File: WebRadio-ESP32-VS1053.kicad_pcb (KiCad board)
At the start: 2 copper layers, 91.5 x 61 mm, 72 parts, among them J1 Conn_01x02, J2 Conn_01x02_Pin, J3 Conn_01x02_Pin, J4 AudioJack3, J5 Conn_01x02_Pin, SW1 SW_Push, SW2 SW_Push, SW3 SW_Push, SW4 SW_Push, U1 AMS1117-1.8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

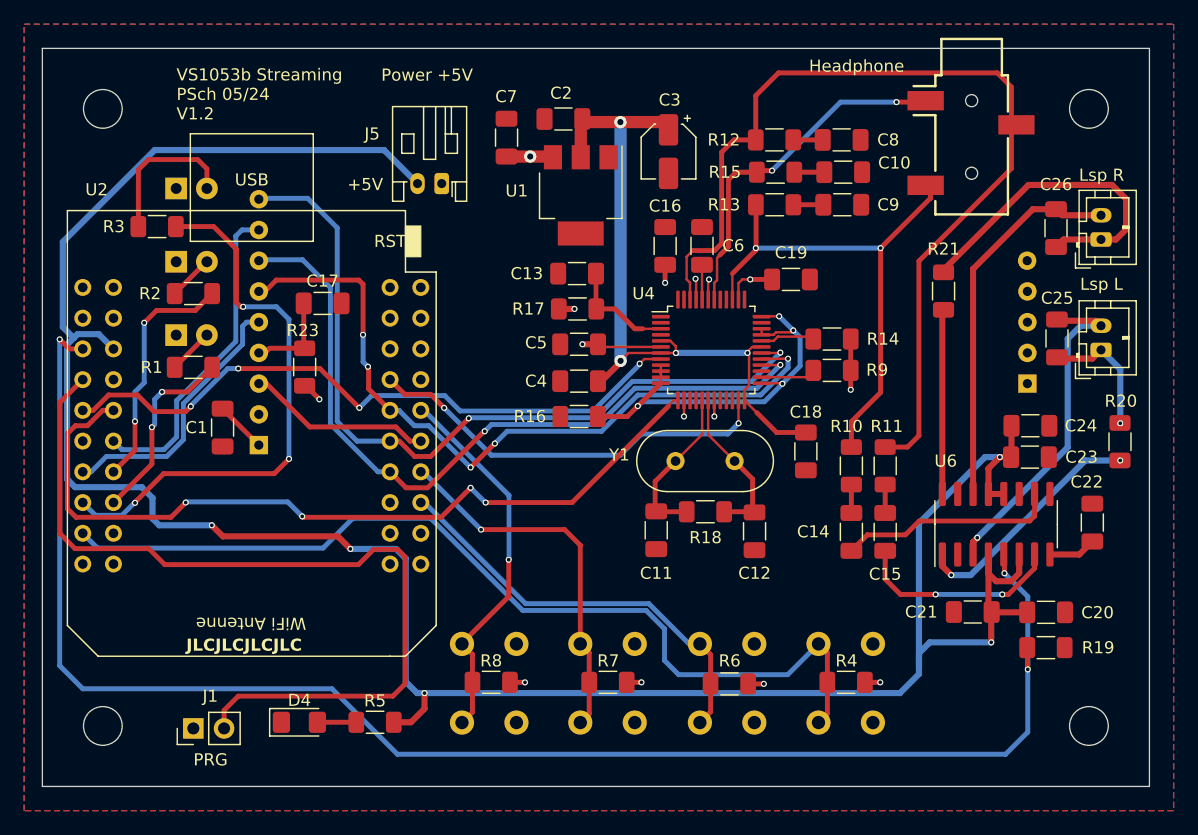
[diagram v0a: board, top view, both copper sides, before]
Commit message: include power over usb-c and jst connector
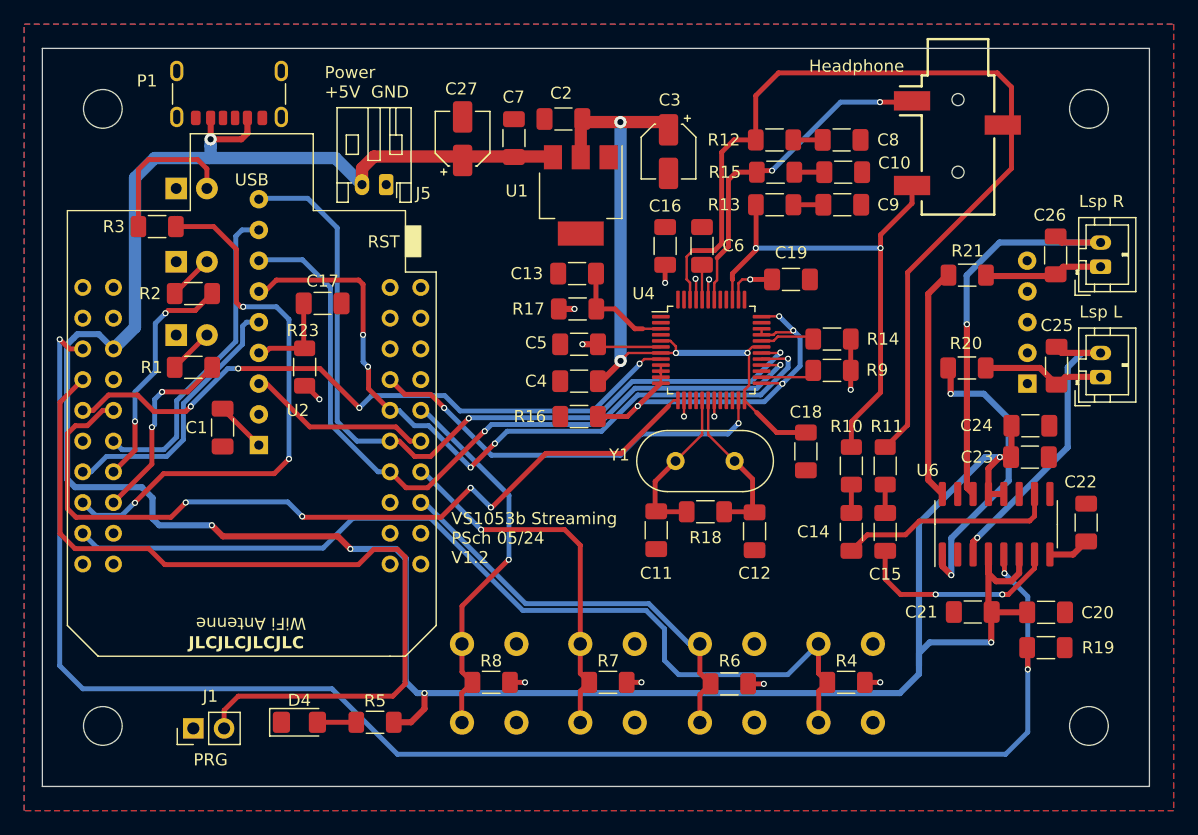
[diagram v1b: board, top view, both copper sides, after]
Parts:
- added C27: 100µF, Capacitor_SMD:CP_Elec_4x5.4, F.Cu at (148.2, 67.5)
- added P1: USB_C_Plug_USB2.0, Connector_USB:USB_C_Receptacle_GCT_USB4125-xx-x_6P_TopMnt_Horizontal, F.Cu at (128.9, 62.7)
- C3: value 10µF -> 47µF
- H1, H2, H3, H4: footprint MountingHole:MountingHole_3.2mm_M3_ISO7380 -> MountingHole:MountingHole_3.2mm_M3_ISO14580
- J4: footprint psch:Jack_3.5mm_SMT_Horizontal -> lib_psch:Jack_3.5mm_SMT_Horizontal
- U2: footprint esp32-mini:ESP32_mini -> ESP32_mini:ESP32_mini
- U5: footprint psch:JLCPCB-Marker -> lib_psch:JLCPCB-Marker
- moved U5 66.3 mm to (130.4, 109.7)
- moved R20 14.0 mm to (189.9, 86.4), turned to 180 degrees
- moved J5 4.59 mm to (141.9, 71.3)
- moved R21 2.36 mm to (189.9, 78.7), turned to 180 degrees
- moved C25 2.25 mm to (197.3, 86.2)
- moved C26 2.25 mm to (197.2, 77.1)
- moved J2 2.25 mm to (201.0, 87.2)
- moved J3 2.25 mm to (201.0, 78.0)
- moved J4 1.13 mm to (189.2, 59.2)
- moved C7 0.61 mm to (152.5, 67.4)
- moved C22 0.51 mm to (199.8, 99.2)
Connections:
- net Net-(U1-VO) renamed +1.8V
- C7 pad 1: +3.3V -> +5V
- U1 pad 3: +3.3V -> +5V
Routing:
- net +5V: track 201.3 -> 220.1 mm, vias 5 -> 6
- net Net-(J3-Pin_1): track 27.6 -> 9.82 mm
- net Net-(U6-LOUT+): track 19.9 -> 24.7 mm
- net Net-(U6-ROUT+): track 15.3 -> 19.4 mm
- net +3.3V: track 39.1 -> 35.1 mm, vias 15 -> 14
- net Net-(J3-Pin_2): track 31.4 -> 34.4 mm, vias 0 -> 1
- net Net-(J2-Pin_2): track 28.1 -> 25.7 mm
- net Net-(U4-GBUF): track 30.9 -> 29.4 mm
- net Net-(U4-LEFT): track 79.0 -> 77.9 mm
- net LED_02: track 20.0 -> 19.4 mm
- net Net-(U4-RIGHT): track 43.7 -> 43.2 mm
- net Net-(U6-VREF): track 3.95 -> 3.44 mm
- net Net-(J2-Pin_1): track 11.2 -> 10.9 mm, vias 1 -> 0
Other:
- board text added: "Power +5V GND"
- board text removed: "Power +5V"

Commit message: change some comments
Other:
- board text added: "WebRadio ESP32 PSch 05/24 V1.2"
- board text removed: "VS1053b Streaming PSch 05/24 V1.2"
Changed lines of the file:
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@@
 		)
 	)
-	(gr_text "VS1053b Streaming\nPSch 05/24\nV1.2"
+	(gr_text "WebRadio ESP32\nPSch 05/24\nV1.2"
 		(at 137.922 110.3376 0)
 		(layer "B.SilkS")
@@
 		)
 	)
-	(gr_text "VS1053b Streaming\nPSch 05/24\nV1.2"
-		(at 147.2946 102.6668 0)
+	(gr_text "WebRadio ESP32\nPSch 05/24\nV1.2"
+		(at 148.5392 102.8192 0)
 		(layer "F.SilkS")
 		(effects

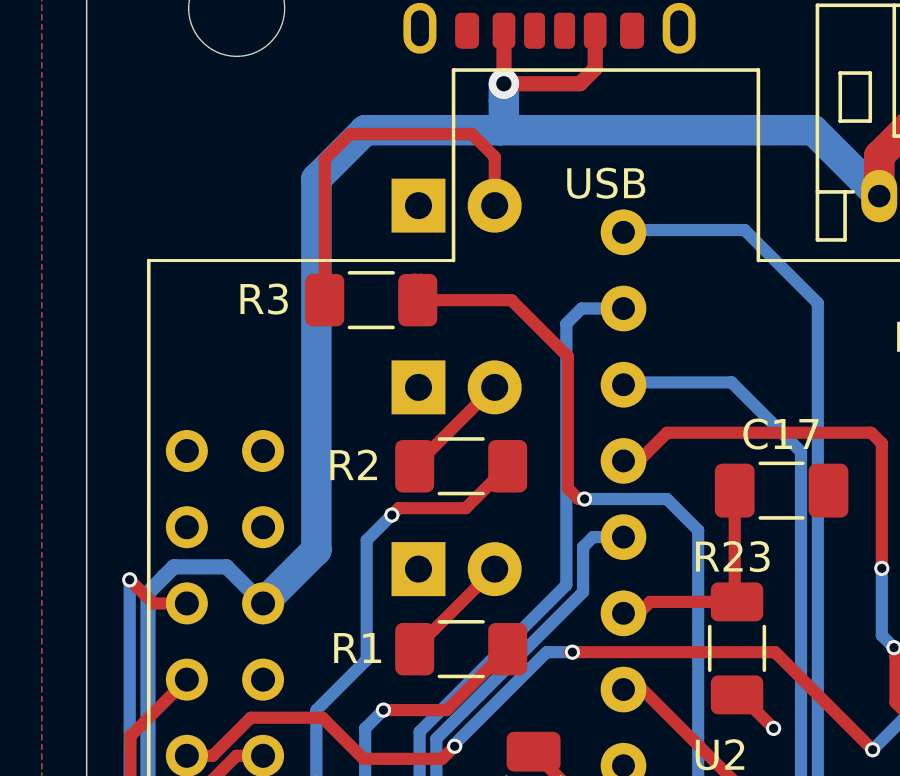
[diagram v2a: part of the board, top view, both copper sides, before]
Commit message: add new footrint for 3mm LED to us also SMD LED's
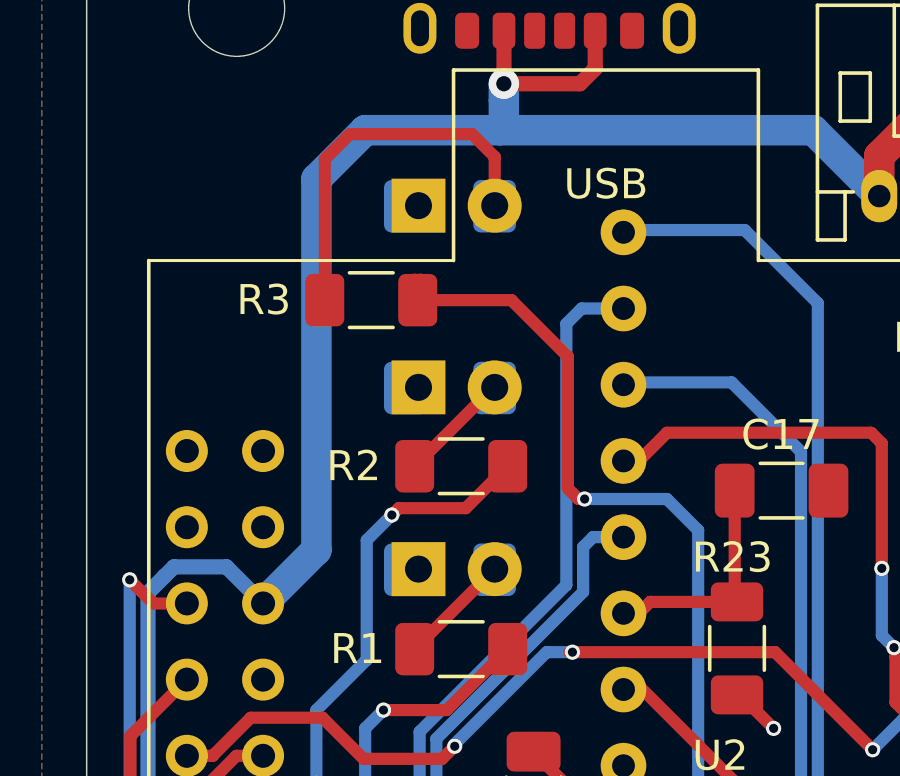
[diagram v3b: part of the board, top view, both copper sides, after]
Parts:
- D1, D2, D3: footprint LED_THT:LED_D3.0mm -> lib_psch:LED_D3.0mm_SMD

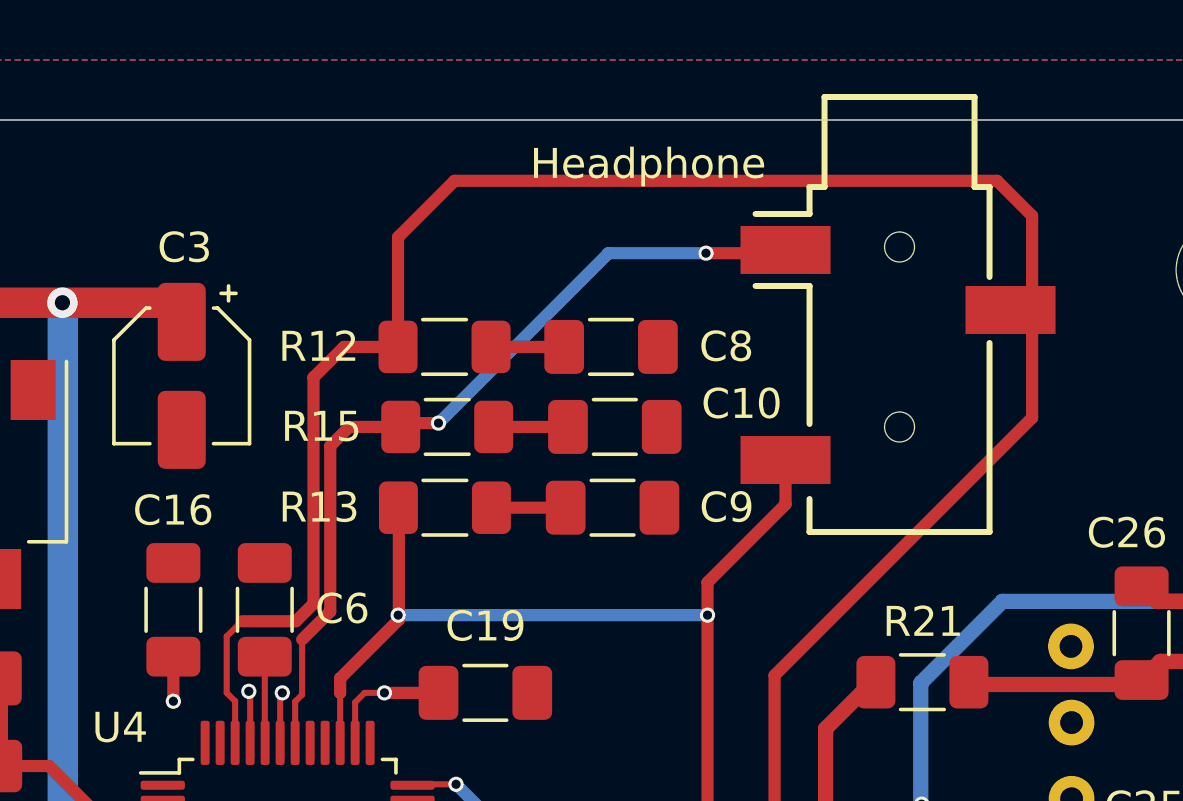
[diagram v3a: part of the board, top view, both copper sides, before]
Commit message: add audio output connector
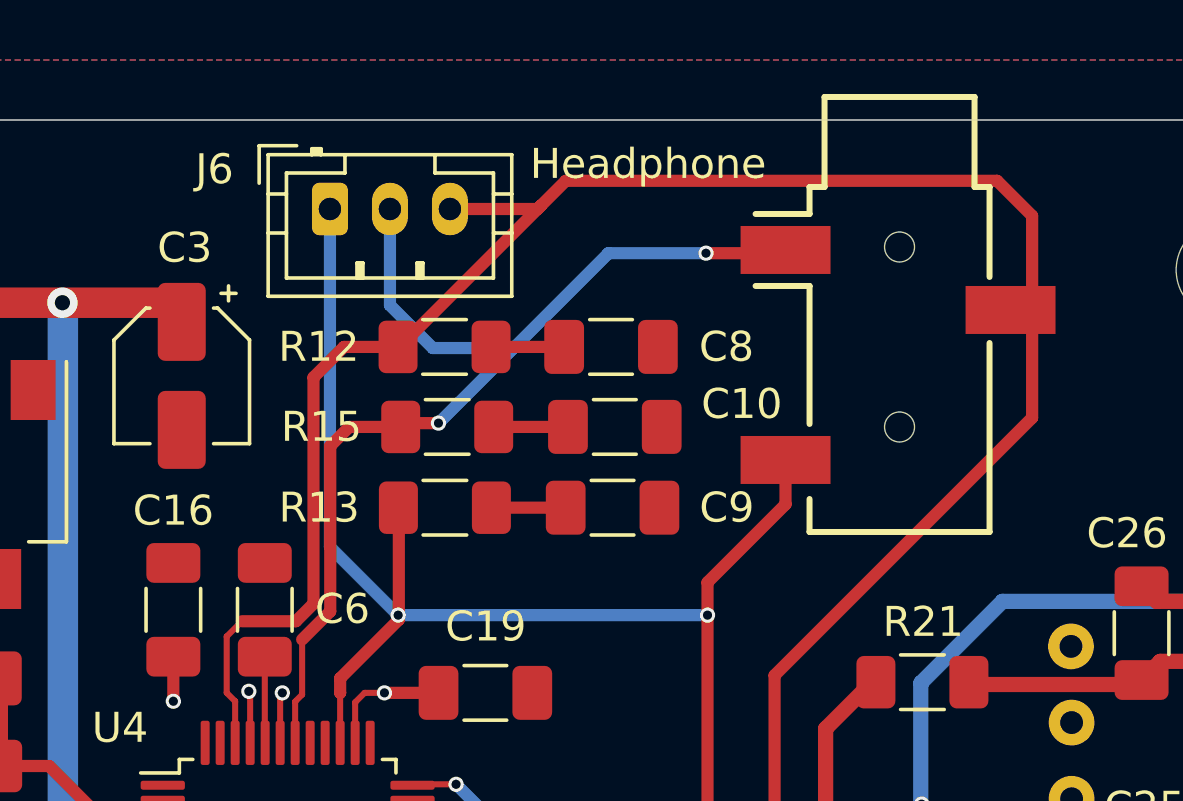
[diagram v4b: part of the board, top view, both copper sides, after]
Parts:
- added J6: JST PH 2mm, Connector_JST:JST_PH_B3B-PH-K_1x03_P2.00mm_Vertical, F.Cu at (170.2, 63.0)
- J2, J3: value Conn_01x02_Pin -> JST PH 2mm
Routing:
- net Net-(J6-Pin_1): track 43.2 -> 57.7 mm
- net Net-(J6-Pin_2): track 29.4 -> 37.3 mm
- net Net-(J6-Pin_3): track 77.9 -> 78.9 mm

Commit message: add labeling
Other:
- board text added: "R G L"
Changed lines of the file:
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@@
+		)
+	)
+	(gr_text "R G L"
+		(at 176.911 64.0842 0)
+		(layer "F.SilkS")
+		(effects
+			(font
+				(size 1 1)
+				(thickness 0.15)
+			)
+			(justify left bottom)
 		)
 	)

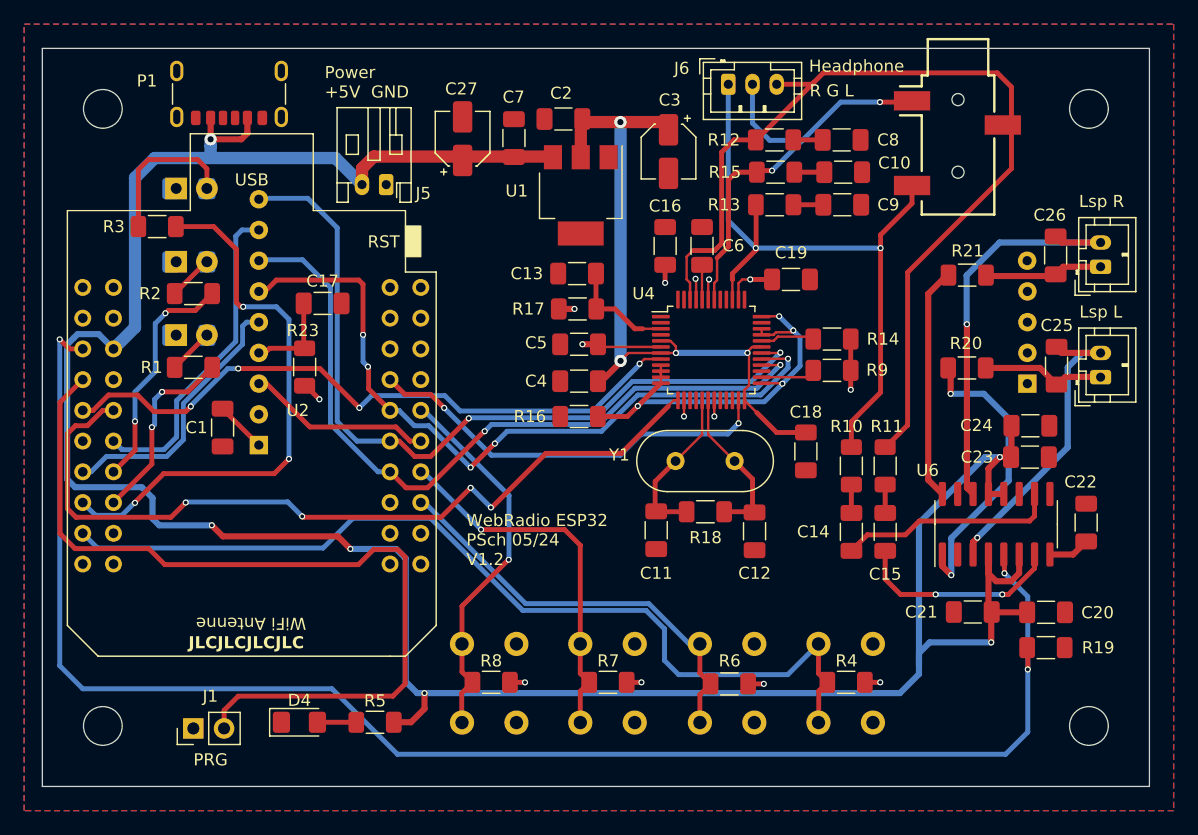
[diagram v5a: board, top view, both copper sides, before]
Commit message: add pin header for leds and swiches
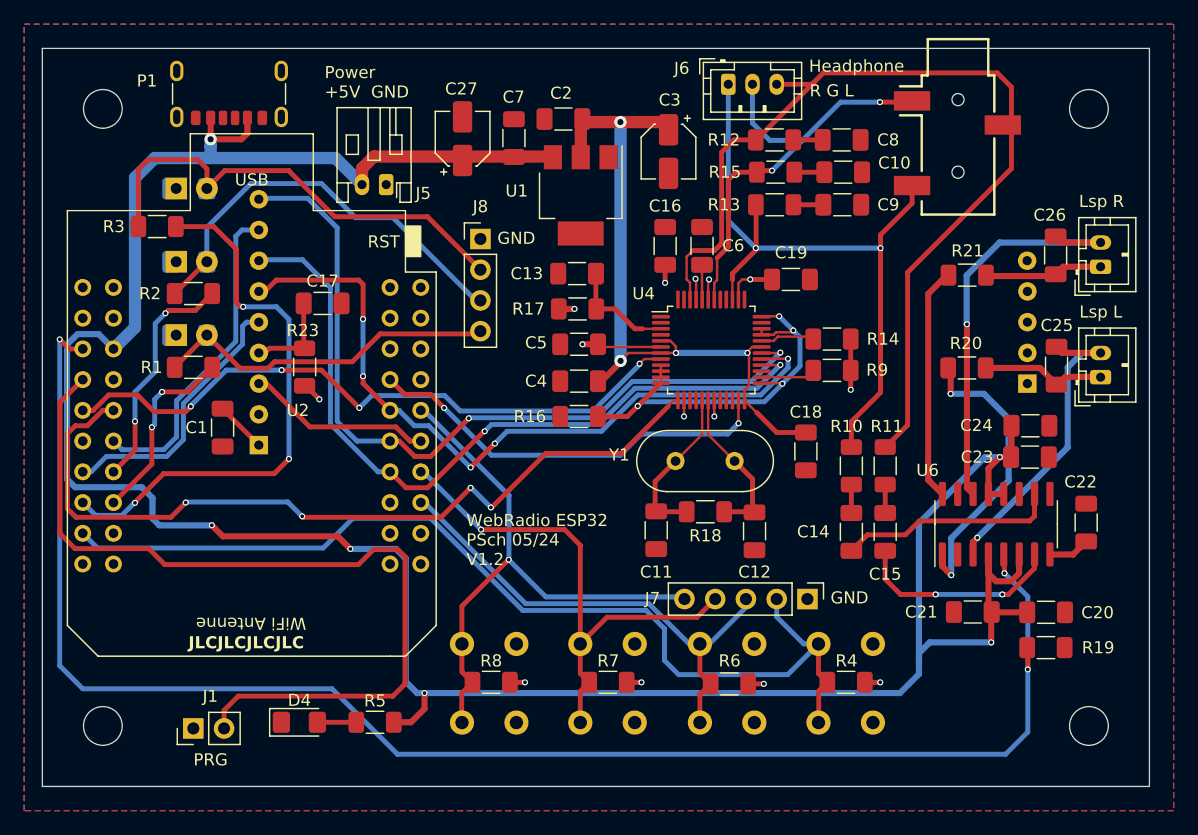
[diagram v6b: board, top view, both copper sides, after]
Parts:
- added J7: Conn_01x05_Pin, Connector_PinHeader_2.54mm:PinHeader_1x05_P2.54mm_Vertical, F.Cu at (176.7, 105.5)
- added J8: Conn_01x04_Pin, Connector_PinHeader_2.54mm:PinHeader_1x04_P2.54mm_Vertical, F.Cu at (149.7, 75.8)
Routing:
- net Net-(D2-A): track 3.79 -> 34.8 mm
- net Net-(D3-A): track 12.9 -> 39.5 mm
- net Net-(D1-A): track 3.77 -> 28.8 mm
- net SW_04: track 31.3 -> 47.5 mm
- net SW_03: track 31.0 -> 43.6 mm
- net SW_01: track 77.4 -> 83.2 mm
- net SW_02: track 35.1 -> 40.9 mm
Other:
- board text added: "D1"
- board text added: "D2"
- board text added: "D3"

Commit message: include JST PH connectors
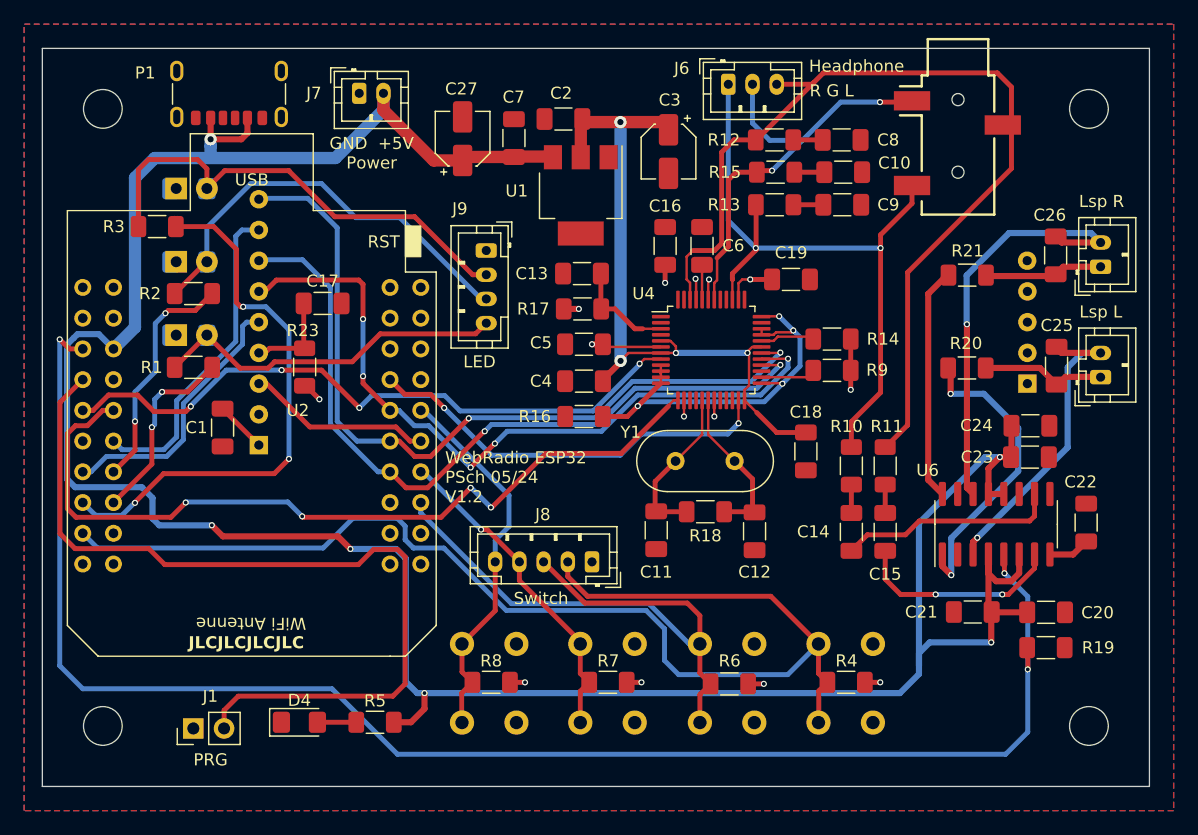
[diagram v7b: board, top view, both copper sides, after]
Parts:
- removed J5: Conn_01x02_Pin, Connector_JST:JST_PH_S2B-PH-K_1x02_P2.00mm_Horizontal
- added J9: Conn_01x04, Connector_JST:JST_PH_B4B-PH-K_1x04_P2.00mm_Vertical, F.Cu at (150.2, 76.7)
- J7: value Conn_01x05_Pin -> JST PH 2mm; footprint Connector_PinHeader_2.54mm:PinHeader_1x05_P2.54mm_Vertical -> Connector_JST:JST_PH_B2B-PH-K_1x02_P2.00mm_Vertical
- J8: value Conn_01x04_Pin -> Conn_01x05; footprint Connector_PinHeader_2.54mm:PinHeader_1x04_P2.54mm_Vertical -> Connector_JST:JST_PH_B5B-PH-K_1x05_P2.00mm_Vertical
- moved J7 55.9 mm to (139.7, 63.7), turned to 0 degrees
- moved J8 28.2 mm to (158.9, 102.4), turned to 180 degrees
- moved C4 0.41 mm to (158.3, 87.5)
- moved C5 0.41 mm to (158.3, 84.5)
- moved R16 0.41 mm to (158.3, 90.4)
- moved C13 0.41 mm to (158.1, 78.6)
- moved R17 0.41 mm to (158.1, 81.5)
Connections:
- net Net-(J6-Pin_1) renamed /RIGHT
- net Net-(J6-Pin_2) renamed /GBUF
- net Net-(J6-Pin_3) renamed /LEFT
- J7 pad 2: SW_01 -> +5V
- J8 pad 2: Net-(D3-A) -> SW_01
- J8 pad 3: Net-(D2-A) -> SW_02
- J8 pad 4: Net-(D1-A) -> SW_03
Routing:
- net SW_01: track 83.2 -> 102.3 mm
- net SW_03: track 43.6 -> 27.2 mm
- net SW_04: track 47.5 -> 31.3 mm, vias 1 -> 0
- net SW_02: track 40.9 -> 53.8 mm
- net +5V: track 220.1 -> 224.3 mm
- net +3.3V: track 35.1 -> 34.3 mm
- net Net-(D1-A): track 28.8 -> 29.5 mm
- net Net-(D3-A): track 39.5 -> 40.1 mm
- net Net-(U6-LOUT+): track 24.7 -> 25.3 mm
- net Net-(J3-Pin_2): track 34.4 -> 35.1 mm
- net LED_03: track 47.4 -> 46.9 mm
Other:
- board text added: "GND +5V Power"
- board text added: "Switch"
- board text removed: "Power +5V GND"
